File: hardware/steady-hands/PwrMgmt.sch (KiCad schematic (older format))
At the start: 30 parts, among them J5 USB_B_Micro, J6 BATT, SW3 SW_SPDT, U6 BQ24075, U7 TPS62841DGR, U8 TPS63001

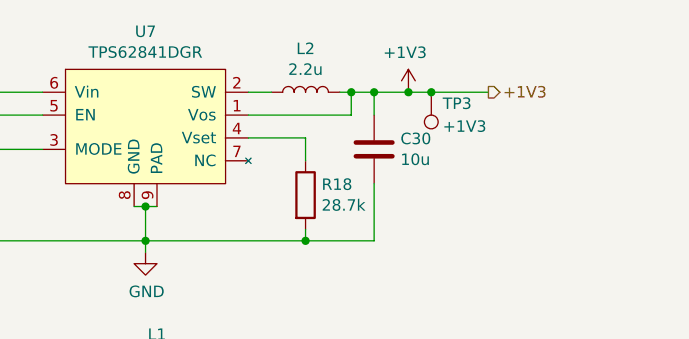
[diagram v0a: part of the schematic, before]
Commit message: Deletes unnecessary files
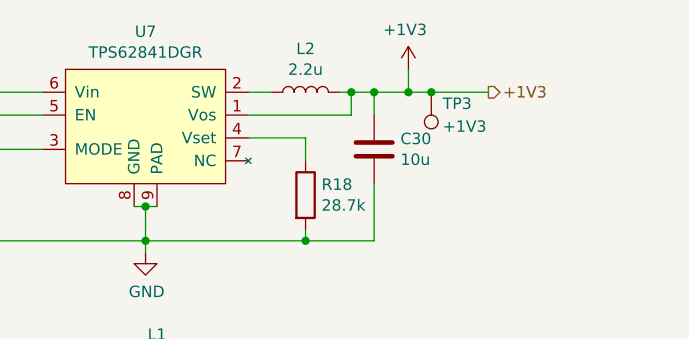
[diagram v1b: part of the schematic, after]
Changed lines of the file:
@@
 Wire Wire Line
 	9650 2550 9750 2550
-Wire Wire Line
-	9750 2550 9900 2550
 Connection ~ 9750 2550
 Wire Wire Line
@@
 	8050 3200 8750 3200
 Connection ~ 8050 3200
-$Comp
-L steady-hands:+1V3 #PWR?
-U 1 1 5F0C6788
-P 9900 2600
-AR Path="/5F0C6788" Ref="#PWR?"  Part="1"
-AR Path="/5F021BD7/5F0C6788" Ref="#PWR0154"  Part="1"
-F 0 "#PWR0154" H 9900 2800 50  0001 C CNN
-F 1 "+1V3" H 9885 2823 50  0000 C CNN
-F 2 "" H 9900 2800 50  0001 C CNN
-F 3 "" H 9900 2800 50  0001 C CNN
-	1    9900 2600
-	1    0    0    -1
-$EndComp
 $Comp
 L power:+3V3 #PWR0155
@@
 	-1   0    0    1
 $EndComp
-Wire Wire Line
-	9900 2550 10000 2550
-Connection ~ 9900 2550
 Connection ~ 10000 2550
 $Comp
@@
 Wire Wire Line
 	10000 2550 10250 2550
+Wire Wire Line
+	9750 2550 9900 2550
+$Comp
+L steady-hands:+1V3 #PWR?
+U 1 1 5F0DA101
+P 9900 2500
+F 0 "#PWR?" H 10000 2500 50  0001 C CNN
+F 1 "+1V3" H 9885 2723 50  0000 C CNN
+F 2 "" H 9900 2500 50  0001 C CNN
+F 3 "" H 9900 2500 50  0001 C CNN
+	1    9900 2500
+	1    0    0    -1
+$EndComp
+Wire Wire Line
+	9900 2450 9900 2550
+Connection ~ 9900 2550
+Wire Wire Line
+	9900 2550 10000 2550
 $EndSCHEMATC

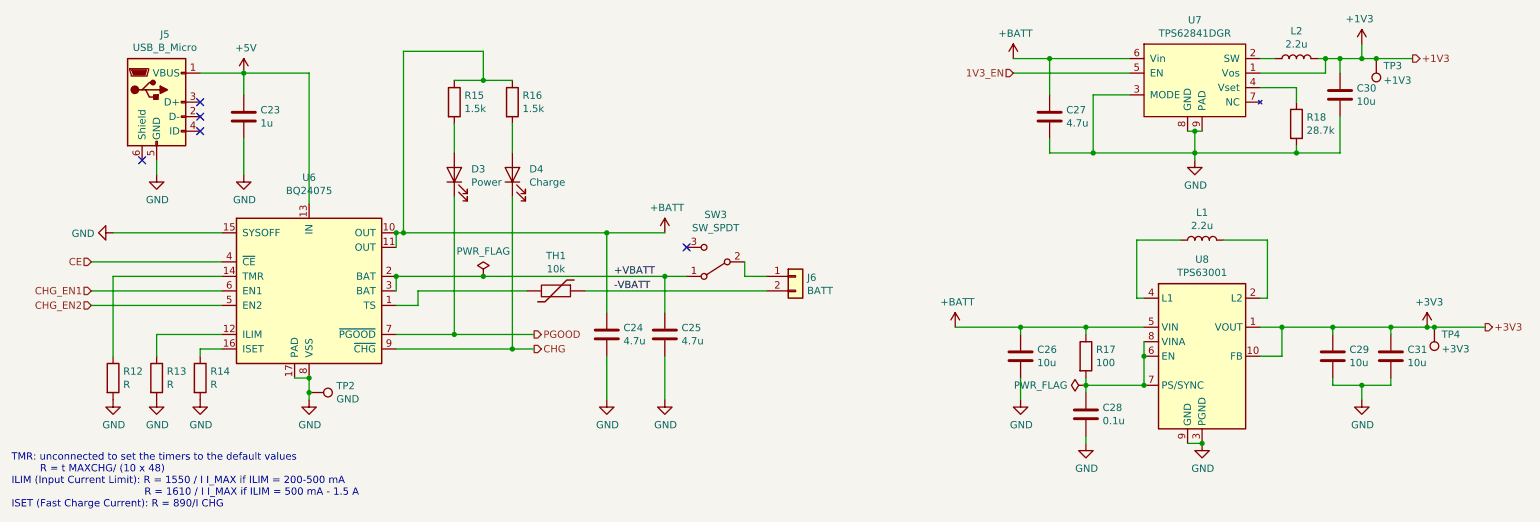
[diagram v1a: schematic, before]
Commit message: Adds footprints
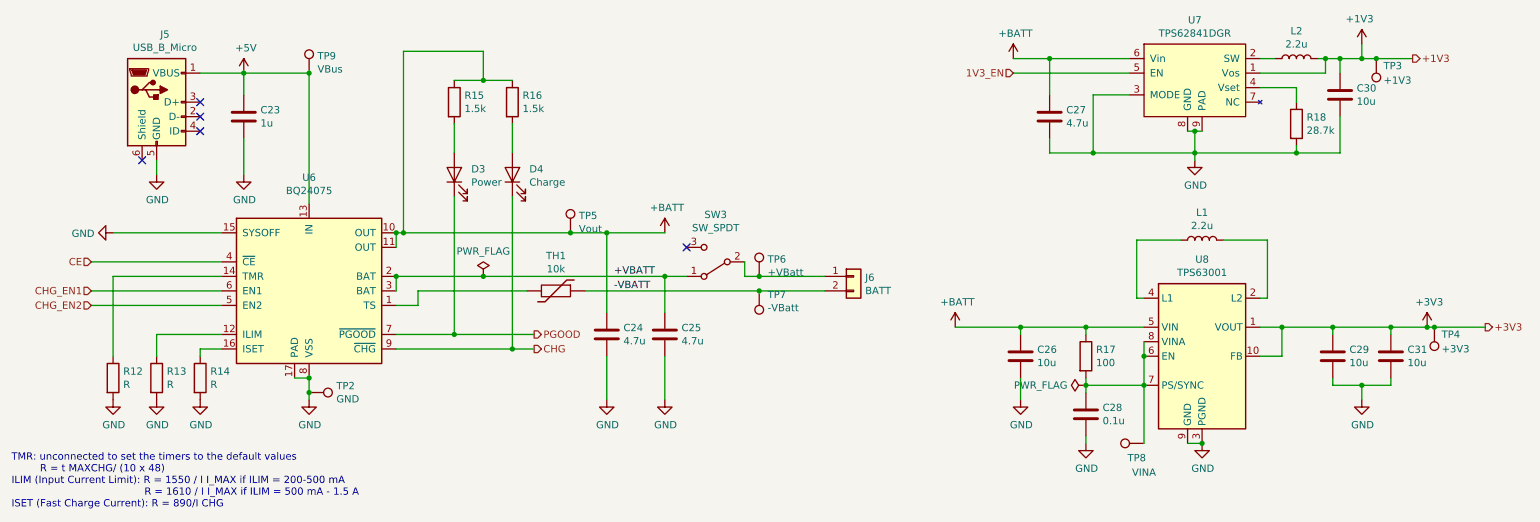
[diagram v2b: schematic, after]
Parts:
- added TP5: Vout, TestPoint:TestPoint_Pad_D1.0mm, symbol Connector:TestPoint
- added TP6: +VBatt, TestPoint:TestPoint_Pad_D1.0mm, symbol Connector:TestPoint
- added TP7: -VBatt, TestPoint:TestPoint_Pad_D1.0mm, symbol Connector:TestPoint
- added TP8: VINA, TestPoint:TestPoint_Pad_D1.0mm, symbol Connector:TestPoint
- added TP9: VBus, TestPoint:TestPoint_Pad_D1.0mm, symbol Connector:TestPoint
- C23, C24, C25, C26, C27, C28, C29, C30, C31: footprint (none) -> Capacitor_SMD:C_0402_1005Metric
- D3, D4: footprint (none) -> LED_SMD:LED_0402_1005Metric
- J6: footprint (none) -> Connector_JST:JST_PH_B2B-PH-SM4-TB_1x02-1MP_P2.00mm_Vertical
- L1, L2: footprint (none) -> Inductor_SMD:L_0402_1005Metric
- R12, R13, R14, R15, R16, R17, R18, TH1: footprint (none) -> Resistor_SMD:R_0402_1005Metric
- TP3, TP4: footprint (none) -> TestPoint:TestPoint_Pad_D1.0mm
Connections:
- net +5V: now also TP9.1
- net +BATT: now also TP5.1
- net -VBATT: now also TP7.1
- net at J6.1 (Pin_1), SW3.2 (B): now also TP6.1
- net at C28.1, R17.2, U8.6 (EN)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: now also TP8.1
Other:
- moved on the sheet: J6
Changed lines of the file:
@@
 $Descr A4 11693 8268
 encoding utf-8
-Sheet 6 7
+Sheet 5 6
 Title ""
 Date ""
@@
 L Connector_Generic:Conn_01x02 J6
 U 1 1 5EFF19F0
-P 6000 4050
-F 0 "J6" H 6080 4042 50  0000 L CNN
-F 1 "BATT" H 6080 3951 50  0000 L CNN
-F 2 "" H 6000 4050 50  0001 C CNN
-F 3 "~" H 6000 4050 50  0001 C CNN
-	1    6000 4050
+P 6400 4050
+F 0 "J6" H 6480 4042 50  0000 L CNN
+F 1 "BATT" H 6480 3951 50  0000 L CNN
+F 2 "Connector_JST:JST_PH_B2B-PH-SM4-TB_1x02-1MP_P2.00mm_Vertical" H 6400 4050 50  0001 C CNN
+F 3 "~" H 6400 4050 50  0001 C CNN
+	1    6400 4050
 	1    0    0    -1
 $EndComp
@@
 F 0 "C25" H 5215 4496 50  0000 L CNN
 F 1 "4.7u" H 5215 4405 50  0000 L CNN
-F 2 "" H 5138 4300 50  0001 C CNN
+F 2 "Capacitor_SMD:C_0402_1005Metric" H 5138 4300 50  0001 C CNN
 F 3 "~" H 5100 4450 50  0001 C CNN
 	1    5100 4450
@@
 F 0 "D3" V 3689 3233 50  0000 R CNN
 F 1 "Power" V 3598 3233 50  0000 R CNN
-F 2 "" H 3650 3350 50  0001 C CNN
+F 2 "LED_SMD:LED_0402_1005Metric" H 3650 3350 50  0001 C CNN
 F 3 "~" H 3650 3350 50  0001 C CNN
 	1    3650 3350
@@
 F 0 "D4" V 4089 3233 50  0000 R CNN
 F 1 "Charge" V 3998 3233 50  0000 R CNN
-F 2 "" H 4050 3350 50  0001 C CNN
+F 2 "LED_SMD:LED_0402_1005Metric" H 4050 3350 50  0001 C CNN
 F 3 "~" H 4050 3350 50  0001 C CNN
 	1    4050 3350
@@
 F 0 "R15" H 3720 2896 50  0000 L CNN
 F 1 "1.5k" H 3720 2805 50  0000 L CNN
-F 2 "" V 3580 2850 50  0001 C CNN
+F 2 "Resistor_SMD:R_0402_1005Metric" V 3580 2850 50  0001 C CNN
 F 3 "~" H 3650 2850 50  0001 C CNN
 	1    3650 2850
@@
 F 0 "R16" H 4120 2896 50  0000 L CNN
 F 1 "1.5k" H 4120 2805 50  0000 L CNN
-F 2 "" V 3980 2850 50  0001 C CNN
+F 2 "Resistor_SMD:R_0402_1005Metric" V 3980 2850 50  0001 C CNN
 F 3 "~" H 4050 2850 50  0001 C CNN
 	1    4050 2850
@@
 Connection ~ 3300 3750
 Wire Wire Line
-	3300 3750 4700 3750
+	3300 3750 4450 3750
 $Comp
 L Device:C C24
@@
 F 0 "C24" H 4815 4496 50  0000 L CNN
 F 1 "4.7u" H 4815 4405 50  0000 L CNN
-F 2 "" H 4738 4300 50  0001 C CNN
+F 2 "Capacitor_SMD:C_0402_1005Metric" H 4738 4300 50  0001 C CNN
 F 3 "~" H 4700 4450 50  0001 C CNN
 	1    4700 4450
@@
 F 0 "R12" H 1370 4796 50  0000 L CNN
 F 1 "R" H 1370 4705 50  0000 L CNN
-F 2 "" V 1230 4750 50  0001 C CNN
+F 2 "Resistor_SMD:R_0402_1005Metric" V 1230 4750 50  0001 C CNN
 F 3 "~" H 1300 4750 50  0001 C CNN
 	1    1300 4750
@@
 F 0 "R13" H 1670 4796 50  0000 L CNN
 F 1 "R" H 1670 4705 50  0000 L CNN
-F 2 "" V 1530 4750 50  0001 C CNN
+F 2 "Resistor_SMD:R_0402_1005Metric" V 1530 4750 50  0001 C CNN
 F 3 "~" H 1600 4750 50  0001 C CNN
 	1    1600 4750
@@
 F 0 "R14" H 1970 4796 50  0000 L CNN
 F 1 "R" H 1970 4705 50  0000 L CNN
-F 2 "" V 1830 4750 50  0001 C CNN
+F 2 "Resistor_SMD:R_0402_1005Metric" V 1830 4750 50  0001 C CNN
 F 3 "~" H 1900 4750 50  0001 C CNN
 	1    1900 4750
@@
 F 0 "C23" H 2315 2996 50  0000 L CNN
 F 1 "1u" H 2315 2905 50  0000 L CNN
-F 2 "" H 2238 2800 50  0001 C CNN
+F 2 "Capacitor_SMD:C_0402_1005Metric" H 2238 2800 50  0001 C CNN
 F 3 "~" H 2200 2950 50  0001 C CNN
 	1    2200 2950
@@
 F 0 "TH1" V 4108 4150 50  0000 C CNN
 F 1 "10k" V 4199 4150 50  0000 C CNN
-F 2 "" H 4350 4150 50  0001 C CNN
+F 2 "Resistor_SMD:R_0402_1005Metric" H 4350 4150 50  0001 C CNN
 F 3 "~" H 4350 4150 50  0001 C CNN
 	1    4350 4150
@@
 F 0 "C26" H 7665 4646 50  0000 L CNN
 F 1 "10u" H 7665 4555 50  0000 L CNN
-F 2 "" H 7588 4450 50  0001 C CNN
+F 2 "Capacitor_SMD:C_0402_1005Metric" H 7588 4450 50  0001 C CNN
 F 3 "~" H 7550 4600 50  0001 C CNN
 	1    7550 4600
@@
 F 0 "R17" H 8070 4646 50  0000 L CNN
 F 1 "100" H 8070 4555 50  0000 L CNN
-F 2 "" V 7930 4600 50  0001 C CNN
+F 2 "Resistor_SMD:R_0402_1005Metric" V 7930 4600 50  0001 C CNN
 F 3 "~" H 8000 4600 50  0001 C CNN
 	1    8000 4600
@@
 F 0 "C28" H 8115 5046 50  0000 L CNN
 F 1 "0.1u" H 8115 4955 50  0000 L CNN
-F 2 "" H 8038 4850 50  0001 C CNN
+F 2 "Capacitor_SMD:C_0402_1005Metric" H 8038 4850 50  0001 C CNN
 F 3 "~" H 8000 5000 50  0001 C CNN
 	1    8000 5000
@@
 F 0 "L1" V 8990 3800 50  0000 C CNN
 F 1 "2.2u" V 8899 3800 50  0000 C CNN
-F 2 "" H 8800 3800 50  0001 C CNN
+F 2 "Inductor_SMD:L_0402_1005Metric" H 8800 3800 50  0001 C CNN
 F 3 "~" H 8800 3800 50  0001 C CNN
 	1    8800 3800
@@
 F 0 "C29" H 9815 4646 50  0000 L CNN
 F 1 "10u" H 9815 4555 50  0000 L CNN
-F 2 "" H 9738 4450 50  0001 C CNN
+F 2 "Capacitor_SMD:C_0402_1005Metric" H 9738 4450 50  0001 C CNN
 F 3 "~" H 9700 4600 50  0001 C CNN
 	1    9700 4600
@@
 F 0 "C31" H 10215 4646 50  0000 L CNN
 F 1 "10u" H 10215 4555 50  0000 L CNN
-F 2 "" H 10138 4450 50  0001 C CNN
+F 2 "Capacitor_SMD:C_0402_1005Metric" H 10138 4450 50  0001 C CNN
 F 3 "~" H 10100 4600 50  0001 C CNN
 	1    10100 4600
@@
 F 0 "L2" V 9640 2550 50  0000 C CNN
 F 1 "2.2u" V 9549 2550 50  0000 C CNN
-F 2 "" H 9450 2550 50  0001 C CNN
+F 2 "Inductor_SMD:L_0402_1005Metric" H 9450 2550 50  0001 C CNN
 F 3 "~" H 9450 2550 50  0001 C CNN
 	1    9450 2550
@@
 F 0 "C30" H 9865 2846 50  0000 L CNN
 F 1 "10u" H 9865 2755 50  0000 L CNN
-F 2 "" H 9788 2650 50  0001 C CNN
+F 2 "Capacitor_SMD:C_0402_1005Metric" H 9788 2650 50  0001 C CNN
 F 3 "~" H 9750 2800 50  0001 C CNN
 	1    9750 2800
@@
 F 0 "R18" H 9520 3046 50  0000 L CNN
 F 1 "28.7k" H 9520 2955 50  0000 L CNN
-F 2 "" V 9380 3000 50  0001 C CNN
+F 2 "Resistor_SMD:R_0402_1005Metric" V 9380 3000 50  0001 C CNN
 F 3 "~" H 9450 3000 50  0001 C CNN
 	1    9450 3000
@@
 F 0 "C27" H 7865 2996 50  0000 L CNN
 F 1 "4.7u" H 7865 2905 50  0000 L CNN
-F 2 "" H 7788 2800 50  0001 C CNN
+F 2 "Capacitor_SMD:C_0402_1005Metric" H 7788 2800 50  0001 C CNN
 F 3 "~" H 7750 2950 50  0001 C CNN
 	1    7750 2950
@@
 $EndComp
 Wire Wire Line
-	4550 4150 5800 4150
+	4550 4150 5750 4150
 Wire Wire Line
 	5650 3950 5650 4050
 Wire Wire Line
-	5650 4050 5800 4050
+	5650 4050 5750 4050
 Text Notes 600  5650 0    50   ~ 0
 TMR: unconnected to set the timers to the default values\n         R = t MAXCHG/ (10 x 48)\nILIM (Input Current Limit): R = 1550 / I I_MAX if ILIM = 200-500 mA\n                                          R = 1610 / I I_MAX if ILIM = 500 mA - 1.5 A\nISET (Fast Charge Current): R = 890/I CHG
@@
 F 0 "TP3" H 9950 2600 50  0000 R CNN
 F 1 "+1V3" H 9950 2700 50  0000 R CNN
-F 2 "" H 10200 2550 50  0001 C CNN
+F 2 "TestPoint:TestPoint_Pad_D1.0mm" H 10200 2550 50  0001 C CNN
 F 3 "~" H 10200 2550 50  0001 C CNN
 	1    10000 2550
@@
 F 0 "TP4" H 10350 4450 50  0000 R CNN
 F 1 "+3V3" H 10350 4550 50  0000 R CNN
-F 2 "" H 10600 4400 50  0001 C CNN
+F 2 "TestPoint:TestPoint_Pad_D1.0mm" H 10600 4400 50  0001 C CNN
 F 3 "~" H 10600 4400 50  0001 C CNN
 	1    10400 4400
@@
 	9750 2550 9900 2550
 $Comp
-L steady-hands:+1V3 #PWR?
+L steady-hands:+1V3 #PWR0154
 U 1 1 5F0DA101
 P 9900 2500
-F 0 "#PWR?" H 10000 2500 50  0001 C CNN
+F 0 "#PWR0154" H 10000 2500 50  0001 C CNN
 F 1 "+1V3" H 9885 2723 50  0000 C CNN
 F 2 "" H 9900 2500 50  0001 C CNN
@@
 Wire Wire Line
 	9900 2550 10000 2550
+$Comp
+L Connector:TestPoint TP6
+U 1 1 5F0E4E4A
+P 5750 4050
+F 0 "TP6" H 5808 4168 50  0000 L CNN
+F 1 "+VBatt" H 5808 4077 50  0000 L CNN
+F 2 "TestPoint:TestPoint_Pad_D1.0mm" H 5950 4050 50  0001 C CNN
+F 3 "~" H 5950 4050 50  0001 C CNN
+	1    5750 4050
+	1    0    0    -1
+$EndComp
+Connection ~ 5750 4050
+$Comp
+L Connector:TestPoint TP7
+U 1 1 5F0E5F07
+P 5750 4150
+F 0 "TP7" H 5692 4176 50  0000 R CNN
+F 1 "-VBatt" H 5692 4267 50  0000 R CNN
+F 2 "TestPoint:TestPoint_Pad_D1.0mm" H 5950 4150 50  0001 C CNN
+F 3 "~" H 5950 4150 50  0001 C CNN
+	1    5750 4150
+	-1   0    0    1
+$EndComp
+Connection ~ 5750 4150
+Wire Wire Line
+	5750 4050 6200 4050
+Wire Wire Line
+	5750 4150 6200 4150
+$Comp
+L Connector:TestPoint TP5
+U 1 1 5F0EDCFE
+P 4450 3750
+F 0 "TP5" H 4508 3868 50  0000 L CNN
+F 1 "Vout" H 4508 3777 50  0000 L CNN
+F 2 "TestPoint:TestPoint_Pad_D1.0mm" H 4650 3750 50  0001 C CNN
+F 3 "~" H 4650 3750 50  0001 C CNN
+	1    4450 3750
+	1    0    0    -1
+$EndComp
+Connection ~ 4450 3750
+Wire Wire Line
+	4450 3750 4700 3750
+$Comp
+L Connector:TestPoint TP8
+U 1 1 5F0EE7C3
+P 8400 5200
+F 0 "TP8" V 8300 5250 50  0000 C CNN
+F 1 "VINA" V 8200 5200 50  0000 C CNN
+F 2 "TestPoint:TestPoint_Pad_D1.0mm" H 8600 5200 50  0001 C CNN
+F 3 "~" H 8600 5200 50  0001 C CNN
+	1    8400 5200
+	0    -1   -1   0
+$EndComp
+Wire Wire Line
+	8400 4800 8400 5200
+$Comp
+L Connector:TestPoint TP9
+U 1 1 5F0F44A4
+P 2650 2650
+F 0 "TP9" H 2708 2768 50  0000 L CNN
+F 1 "VBus" H 2708 2677 50  0000 L CNN
+F 2 "TestPoint:TestPoint_Pad_D1.0mm" H 2850 2650 50  0001 C CNN
+F 3 "~" H 2850 2650 50  0001 C CNN
+	1    2650 2650
+	1    0    0    -1
+$EndComp
+Connection ~ 2650 2650
 $EndSCHEMATC

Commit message: Adds IC footprints
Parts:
- J5: footprint (none) -> Connector_USB:USB_Micro-B_Molex-105017-0001
- U6: footprint (none) -> Package_DFN_QFN:QFN-16-1EP_3x3mm_P0.5mm_EP1.7x1.7mm
- U7: footprint (none) -> Sij_Package_SO:HVSSOP-8-1EP_3x3mm_P0.065mm_EP2.2x3.1mm_Mask1.35x1.65mm
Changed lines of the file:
@@
 F 0 "J5" H 1657 3317 50  0000 C CNN
 F 1 "USB_B_Micro" H 1657 3226 50  0000 C CNN
-F 2 "" H 1750 2800 50  0001 C CNN
+F 2 "Connector_USB:USB_Micro-B_Molex-105017-0001" H 1750 2800 50  0001 C CNN
 F 3 "~" H 1750 2800 50  0001 C CNN
 	1    1600 2850
@@
 F 0 "U6" H 2650 4931 50  0000 C CNN
 F 1 "BQ24075" H 2650 4840 50  0000 C CNN
-F 2 "" H 2900 3600 50  0001 L CNN
+F 2 "Package_DFN_QFN:QFN-16-1EP_3x3mm_P0.5mm_EP1.7x1.7mm" H 2900 3600 50  0001 L CNN
 F 3 "http://www.ti.com/lit/ds/symlink/bq24075.pdf" H 2850 4350 50  0001 C CNN
 	1    2650 4150
@@
 F 0 "U7" H 8750 4215 50  0000 C CNN
 F 1 "TPS62841DGR" H 8750 4124 50  0000 C CNN
-F 2 "" H 8750 3250 50  0001 C CNN
+F 2 "Sij_Package_SO:HVSSOP-8-1EP_3x3mm_P0.065mm_EP2.2x3.1mm_Mask1.35x1.65mm" H 8750 3250 50  0001 C CNN
 F 3 "" H 8750 3250 50  0001 C CNN
 	1    8750 3250

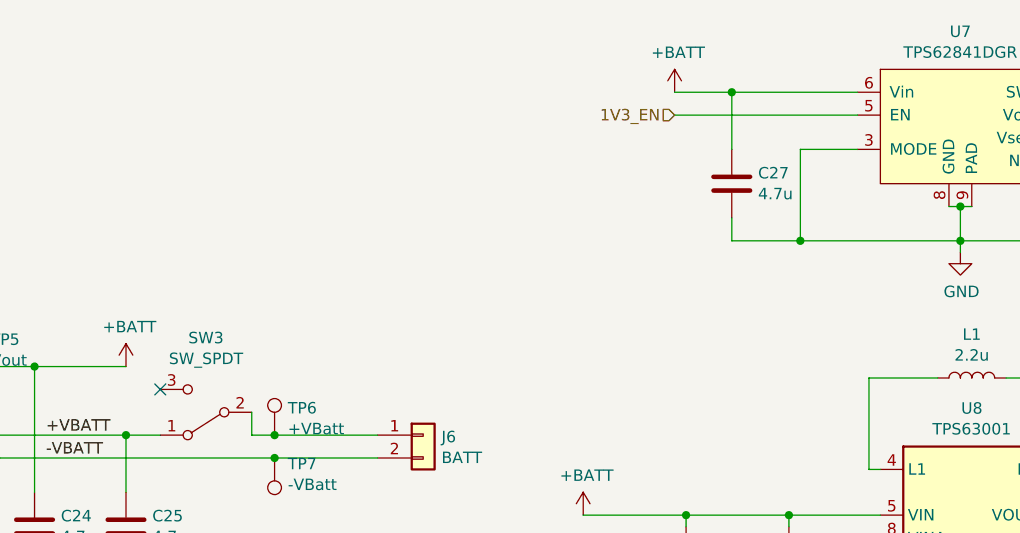
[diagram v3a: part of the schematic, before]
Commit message: Adds all footprints to board
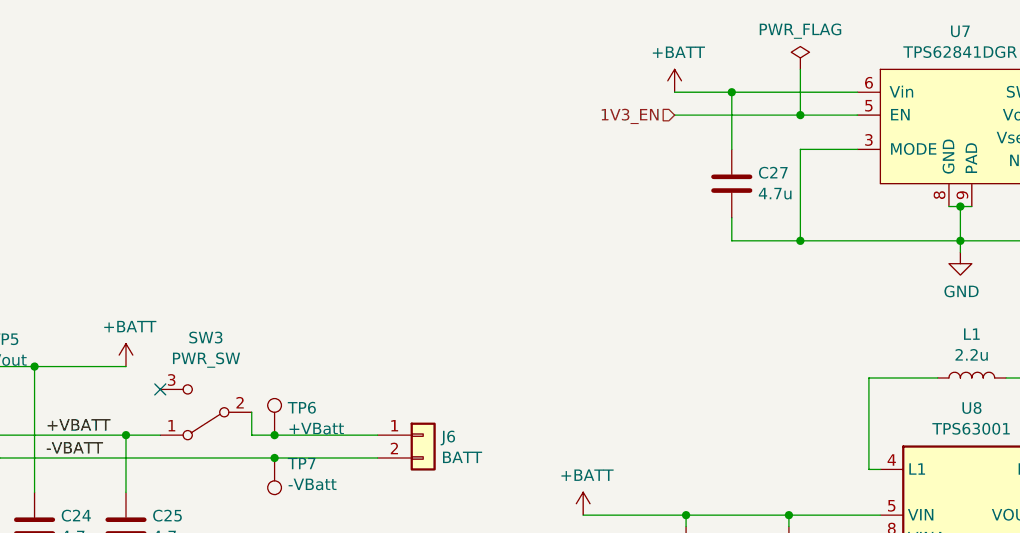
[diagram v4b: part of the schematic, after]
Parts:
- SW3: value SW_SPDT -> PWR_SW; footprint (none) -> Sij_Switches:EG1224
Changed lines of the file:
@@
 	7750 3200 8050 3200
-Wire Wire Line
-	8300 2650 7500 2650
 Wire Wire Line
 	8300 2800 8050 2800
@@
 P 5450 3950
 F 0 "SW3" H 5450 3625 50  0000 C CNN
-F 1 "SW_SPDT" H 5450 3716 50  0000 C CNN
-F 2 "" H 5450 3950 50  0001 C CNN
+F 1 "PWR_SW" H 5450 3716 50  0000 C CNN
+F 2 "Sij_Switches:EG1224" H 5450 3950 50  0001 C CNN
 F 3 "~" H 5450 3950 50  0001 C CNN
 	1    5450 3950
@@
 $EndComp
 Connection ~ 2650 2650
+Wire Wire Line
+	7500 2650 8050 2650
+$Comp
+L power:PWR_FLAG #FLG0101
+U 1 1 5F102C19
+P 8050 2450
+F 0 "#FLG0101" H 8050 2525 50  0001 C CNN
+F 1 "PWR_FLAG" H 8050 2623 50  0000 C CNN
+F 2 "" H 8050 2450 50  0001 C CNN
+F 3 "~" H 8050 2450 50  0001 C CNN
+	1    8050 2450
+	1    0    0    -1
+$EndComp
+Wire Wire Line
+	8050 2450 8050 2650
+Connection ~ 8050 2650
+Wire Wire Line
+	8050 2650 8300 2650
 $EndSCHEMATC
